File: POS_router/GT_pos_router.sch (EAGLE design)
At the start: 72 parts, among them J1 DB25-RA-MALE, J10 HDR_1X4, J2 DB25-RA-FEMALE, J3 RPI_ZERO_HDR0.2_STACK, J4 PWR_JACK_SW_NC, J7 RJ45-JACK-VERT, J8 USB-MICRO-B-SMT-FLG, J9 USB-A-RECEPT-RA, U1 FT2232H, U2 MAX3243ST-EB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

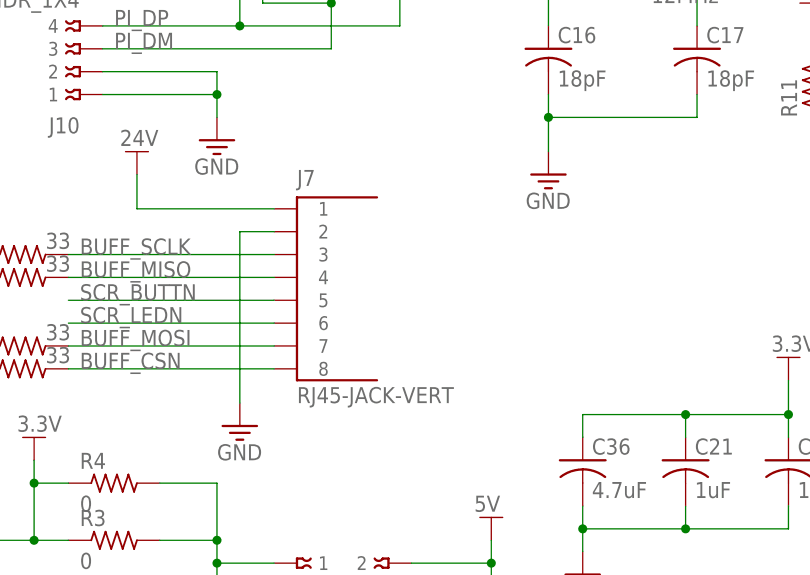
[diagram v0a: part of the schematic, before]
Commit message: Moved RJ45 to edge and made RA
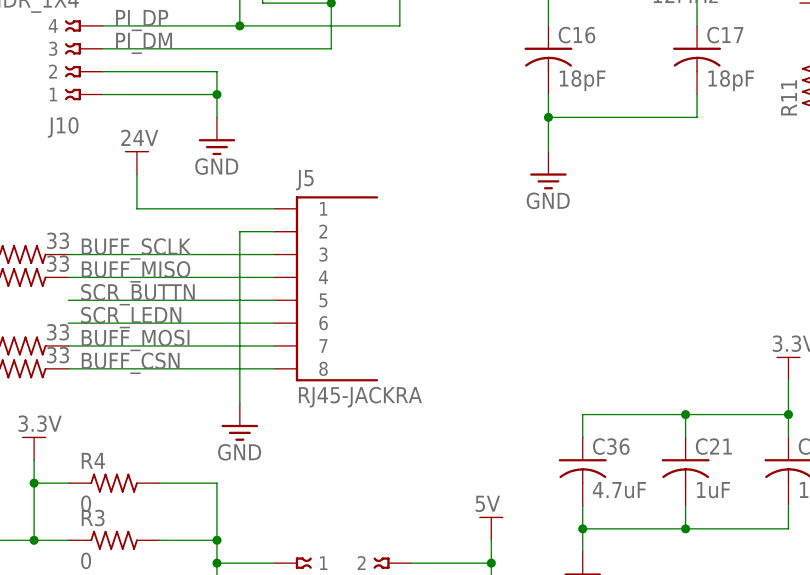
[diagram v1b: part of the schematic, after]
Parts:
- removed J7: RJ45-JACK-VERT, mechanical:RJ45-JACK-VERT
- added J5: RJ45-JACKRA, mechanical:RJ45-JACKRA
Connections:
- net 24V: now also J5.1; no longer J7.1
- net BUFF_CSN: now also J5.8; no longer J7.8
- net BUFF_MISO: now also J5.4; no longer J7.4
- net BUFF_MOSI: now also J5.7; no longer J7.7
- net BUFF_SCLK: now also J5.3; no longer J7.3
- net GND: now also J5.2; no longer J7.2
- net SCR_BUTTN: now also J5.5; no longer J7.5
- net SCR_LEDN: now also J5.6; no longer J7.6
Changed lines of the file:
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@@
 <?xml version="1.0" encoding="utf-8"?>
 <!DOCTYPE eagle SYSTEM "eagle.dtd">
-<eagle version="9.0.1">
+<eagle version="9.1.1">
 <drawing>
 <settings>
@@
 <part name="U3" library="communication" deviceset="MAX3243" device="ST-EB"/>
 <part name="FRAME2" library="frames" deviceset="FRAME_B_L" device=""/>
-<part name="J7" library="mechanical" deviceset="RJ45-JACK-VERT" device=""/>
 <part name="J8" library="mechanical" deviceset="USB" device="-MICRO-B-SMT-FLG"/>
 <part name="J9" library="mechanical" deviceset="USB-A-RECEPT-RA" device=""/>
@@
 <part name="PWR54" library="supply" deviceset="GND" device=""/>
 <part name="PWR55" library="supply" deviceset="GND" device=""/>
+<part name="J5" library="mechanical" deviceset="RJ45-JACK" device="RA"/>
 </parts>
 <sheets>
@@
 <instance part="FRAME2" gate="G$1" x="0" y="0"/>
 <instance part="FRAME2" gate="G$2" x="325.12" y="0"/>
-<instance part="J7" gate="G$1" x="63.5" y="116.84"/>
 <instance part="J8" gate="G$1" x="31.75" y="154.94" rot="MR0"/>
 <instance part="J9" gate="G$1" x="231.14" y="72.39"/>
@@
 <instance part="PWR54" gate="G$1" x="137.16" y="205.74"/>
 <instance part="PWR55" gate="G$1" x="118.11" y="191.77"/>
+<instance part="J5" gate="G$1" x="63.5" y="116.84"/>
 </instances>
 <busses>
@@
 </segment>
 <segment>
-<pinref part="J7" gate="G$1" pin="2"/>
 <wire x1="63.5" y1="116.84" x2="59.69" y2="116.84" width="0.1524" layer="91"/>
 <wire x1="59.69" y1="116.84" x2="59.69" y2="97.79" width="0.1524" layer="91"/>
 <pinref part="PWR45" gate="G$1" pin="GND"/>
+<pinref part="J5" gate="G$1" pin="2"/>
 </segment>
 <segment>
@@
 </segment>
 <segment>
-<pinref part="J7" gate="G$1" pin="1"/>
 <wire x1="63.5" y1="119.38" x2="48.26" y2="119.38" width="0.1524" layer="91"/>
 <wire x1="48.26" y1="119.38" x2="48.26" y2="123.19" width="0.1524" layer="91"/>
 <pinref part="PWR47" gate="G$1" pin="24V"/>
+<pinref part="J5" gate="G$1" pin="1"/>
 </segment>
 </net>
 <net name="SCR_BUTTN" class="0">
 <segment>
-<pinref part="J7" gate="G$1" pin="5"/>
 <wire x1="63.5" y1="109.22" x2="40.64" y2="109.22" width="0.1524" layer="91"/>
 <label x="41.91" y="109.22" size="1.778" layer="95"/>
+<pinref part="J5" gate="G$1" pin="5"/>
 </segment>
 <segment>
@@
 <net name="SCR_LEDN" class="0">
 <segment>
-<pinref part="J7" gate="G$1" pin="6"/>
 <wire x1="63.5" y1="106.68" x2="40.64" y2="106.68" width="0.1524" layer="91"/>
 <label x="41.91" y="106.68" size="1.778" layer="95"/>
+<pinref part="J5" gate="G$1" pin="6"/>
 </segment>
 <segment>
@@
 <net name="BUFF_SCLK" class="0">
 <segment>
-<pinref part="J7" gate="G$1" pin="3"/>
 <wire x1="63.5" y1="114.3" x2="40.64" y2="114.3" width="0.1524" layer="91"/>
 <label x="41.91" y="114.3" size="1.778" layer="95"/>
 <pinref part="R12" gate="G$1" pin="2"/>
+<pinref part="J5" gate="G$1" pin="3"/>
 </segment>
 </net>
 <net name="BUFF_MISO" class="0">
 <segment>
-<pinref part="J7" gate="G$1" pin="4"/>
 <wire x1="63.5" y1="111.76" x2="40.64" y2="111.76" width="0.1524" layer="91"/>
 <label x="41.91" y="111.76" size="1.778" layer="95"/>
 <pinref part="R13" gate="G$1" pin="2"/>
+<pinref part="J5" gate="G$1" pin="4"/>
 </segment>
 </net>
 <net name="BUFF_MOSI" class="0">
 <segment>
-<pinref part="J7" gate="G$1" pin="7"/>
 <wire x1="63.5" y1="104.14" x2="40.64" y2="104.14" width="0.1524" layer="91"/>
 <label x="41.91" y="104.14" size="1.778" layer="95"/>
 <pinref part="R14" gate="G$1" pin="2"/>
+<pinref part="J5" gate="G$1" pin="7"/>
 </segment>
 </net>
 <net name="BUFF_CSN" class="0">
 <segment>
-<pinref part="J7" gate="G$1" pin="8"/>
 <wire x1="63.5" y1="101.6" x2="40.64" y2="101.6" width="0.1524" layer="91"/>
 <label x="41.91" y="101.6" size="1.778" layer="95"/>
 <pinref part="R15" gate="G$1" pin="2"/>
-</segment>
-</net>
+<pinref part="J5" gate="G$1" pin="8"/>
+</segment>
+</net>
